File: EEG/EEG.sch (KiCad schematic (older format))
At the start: 1 part

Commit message: ...
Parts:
- gave numbers to parts that had none: 1
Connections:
- net labels added: +5V, GND
- wire segments 0 -> 3
- no-connect marks 0 -> 2
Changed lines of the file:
@@
 $EndDescr
 $Comp
-L Connector:USB_B_Micro J?
+L Connector:USB_B_Micro J1
 U 1 1 603925D3
 P 1950 2800
-F 0 "J?" H 2007 3267 50  0000 C CNN
+F 0 "J1" H 2007 3267 50  0000 C CNN
 F 1 "USB_B_Micro" H 2007 3176 50  0000 C CNN
 F 2 "" H 2100 2750 50  0001 C CNN
@@
 	1    0    0    -1
 $EndComp
+Wire Wire Line
+	1950 3200 1950 3500
+$Comp
+L power:GND #PWR?
+U 1 1 603940FA
+P 1950 3500
+F 0 "#PWR?" H 1950 3250 50  0001 C CNN
+F 1 "GND" H 1955 3327 50  0000 C CNN
+F 2 "" H 1950 3500 50  0001 C CNN
+F 3 "" H 1950 3500 50  0001 C CNN
+	1    1950 3500
+	1    0    0    -1
+$EndComp
+NoConn ~ 1850 3200
+NoConn ~ 2250 3000
+$Comp
+L power:+5V #PWR?
+U 1 1 60394FDA
+P 2500 2300
+F 0 "#PWR?" H 2500 2150 50  0001 C CNN
+F 1 "+5V" H 2515 2473 50  0000 C CNN
+F 2 "" H 2500 2300 50  0001 C CNN
+F 3 "" H 2500 2300 50  0001 C CNN
+	1    2500 2300
+	1    0    0    -1
+$EndComp
+Wire Wire Line
+	2250 2600 2500 2600
+Wire Wire Line
+	2500 2600 2500 2300
 $EndSCHEMATC

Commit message: added stuff to schematic
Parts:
- added C? (x2): 10uF, symbol Device:CP_Small
- added C? (x4): 0.1uF, symbol Device:CP_Small
- added C?: 2.2uF, symbol Device:CP_Small
- added C? (x8): 100nF, symbol Device:CP_Small
- added D? (x3): D_TVS, symbol Device:D_TVS
- added D?: LED, symbol Device:LED
- added D?: D_Schottky_Small, symbol Device:D_Schottky_Small
- added Q? (x2): 2N2219, Package_TO_SOT_THT:TO-39-3, symbol Transistor_BJT:2N2219
- added R? (x3): 2K, symbol Device:R_Small_US
- added R? (x4): 0R, symbol Device:R_Small_US
- added R? (x2): 10K, symbol Device:R_Small_US
- added SW? (x2): SW_Push, symbol Switch:SW_Push
- added U?: AMS1117-3.3, Package_TO_SOT_SMD:SOT-223-3_TabPin2, symbol Regulator_Linear:AMS1117-3.3
- added U?: FT231XS, Package_SO:SSOP-20_3.9x8.7mm_P0.635mm, symbol Interface_USB:FT231XS
- added U?: ESP32-PICO-D4, Package_DFN_QFN:QFN-48-1EP_7x7mm_P0.5mm_EP5.3x5.3mm, symbol RF_Module:ESP32-PICO-D4
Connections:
- net labels added: +3.3V, D+, D-, EN, IO0, RXD, TXD
- net labels removed: +5V
- wire segments 3 -> 145
- no-connect marks 2 -> 10
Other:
- note added: "3.3V power Supply"
- note added: "Push buttons\n"
- note added: "USB to UART\n"
- moved on the sheet: J1

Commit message: ...
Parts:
- added R?: 5k, symbol Device:R_Small_US
- added U?: MAX7219, symbol Driver_LED:MAX7219
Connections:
- net +3V3: now also R?.2, U?.19 (V+)
- net GND: now also U?.4 (GND), U?.9 (GND)
- net CS: now reaches U?.34 (IO5)
- net CS: now also U?.12 (LOAD)
- net Sclk: now reaches U?.35 (IO18)
- net Sclk: now also U?.13 (CLK)
- net Data: now reaches U?.36 (IO23)
- net Data: now also U?.1 (DIN)
- new net: R?.1, U?.18 (ISET)
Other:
- moved on the sheet: C?, R?, U?

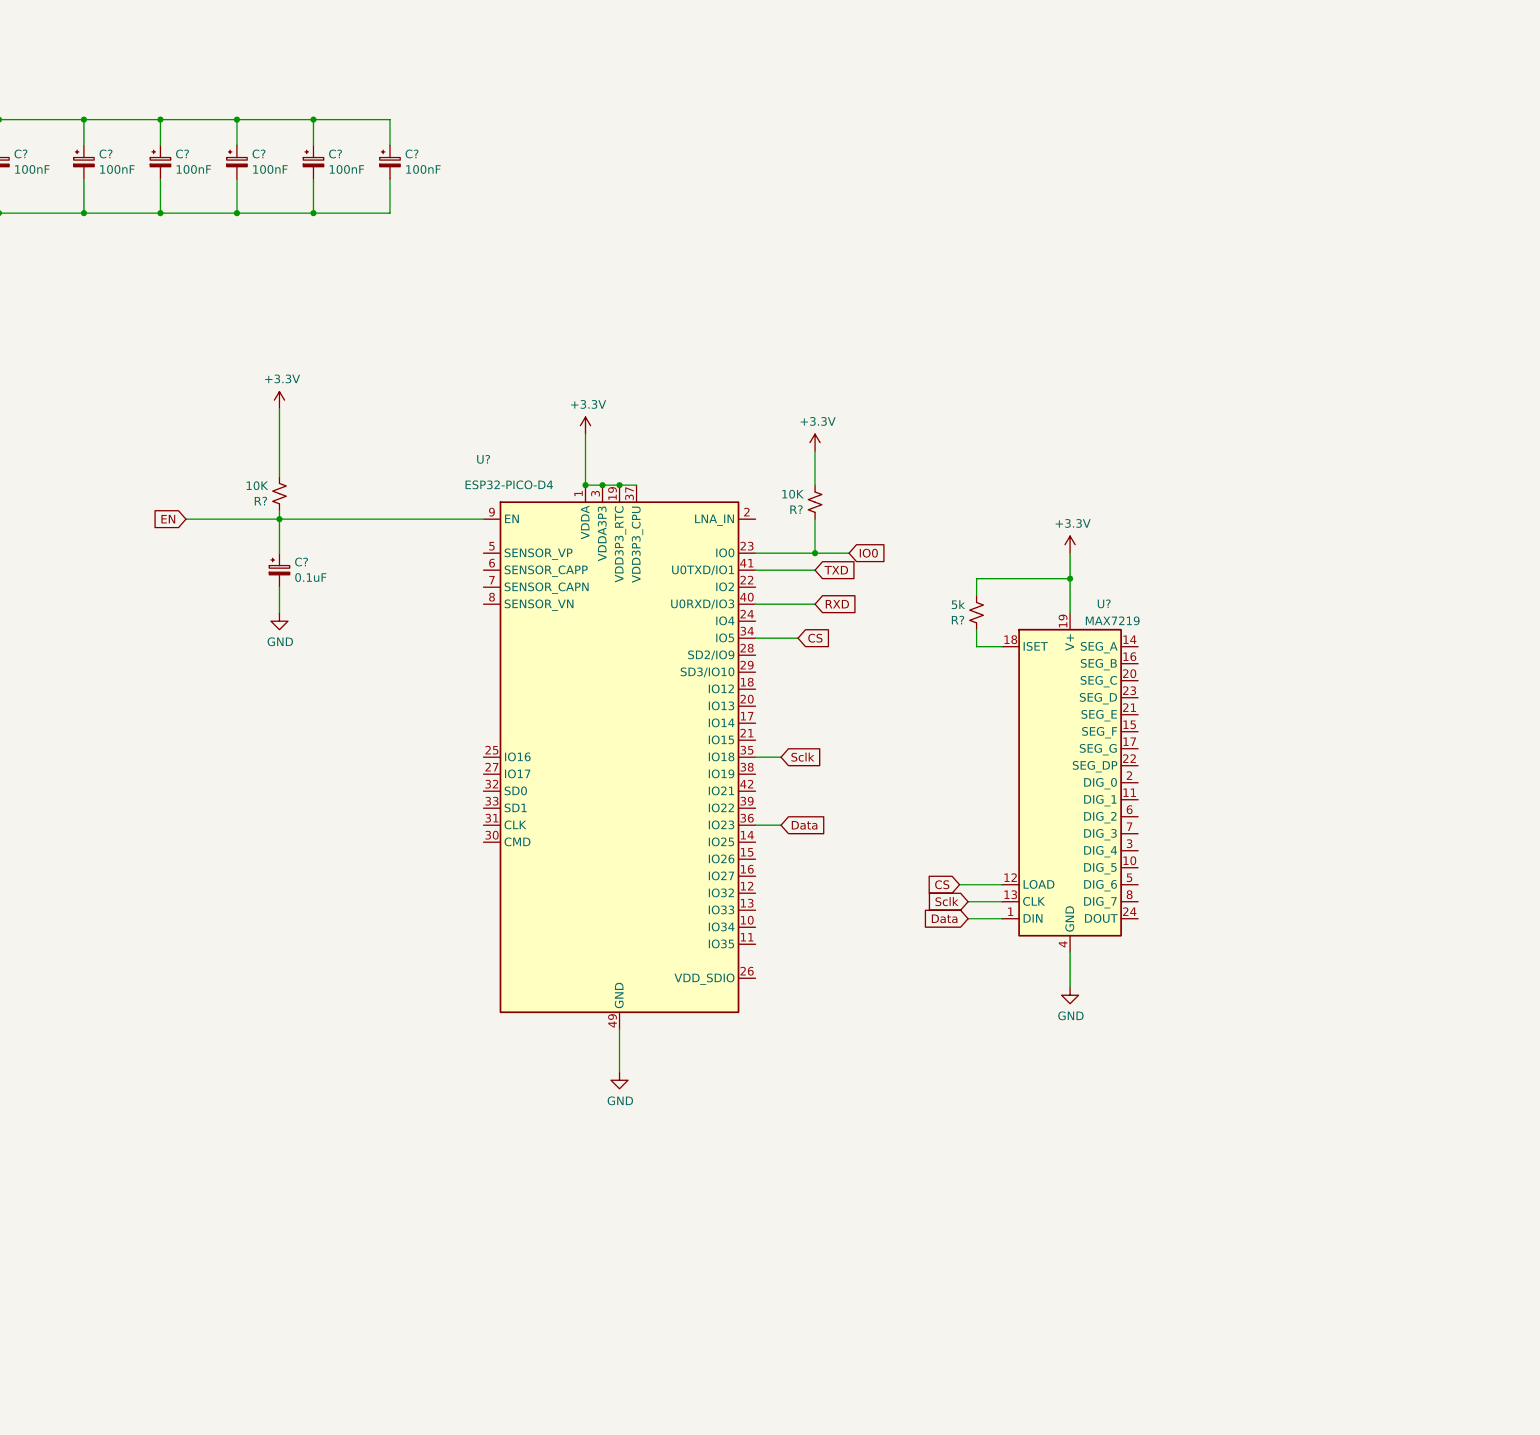
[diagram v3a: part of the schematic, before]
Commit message: ADDED LED
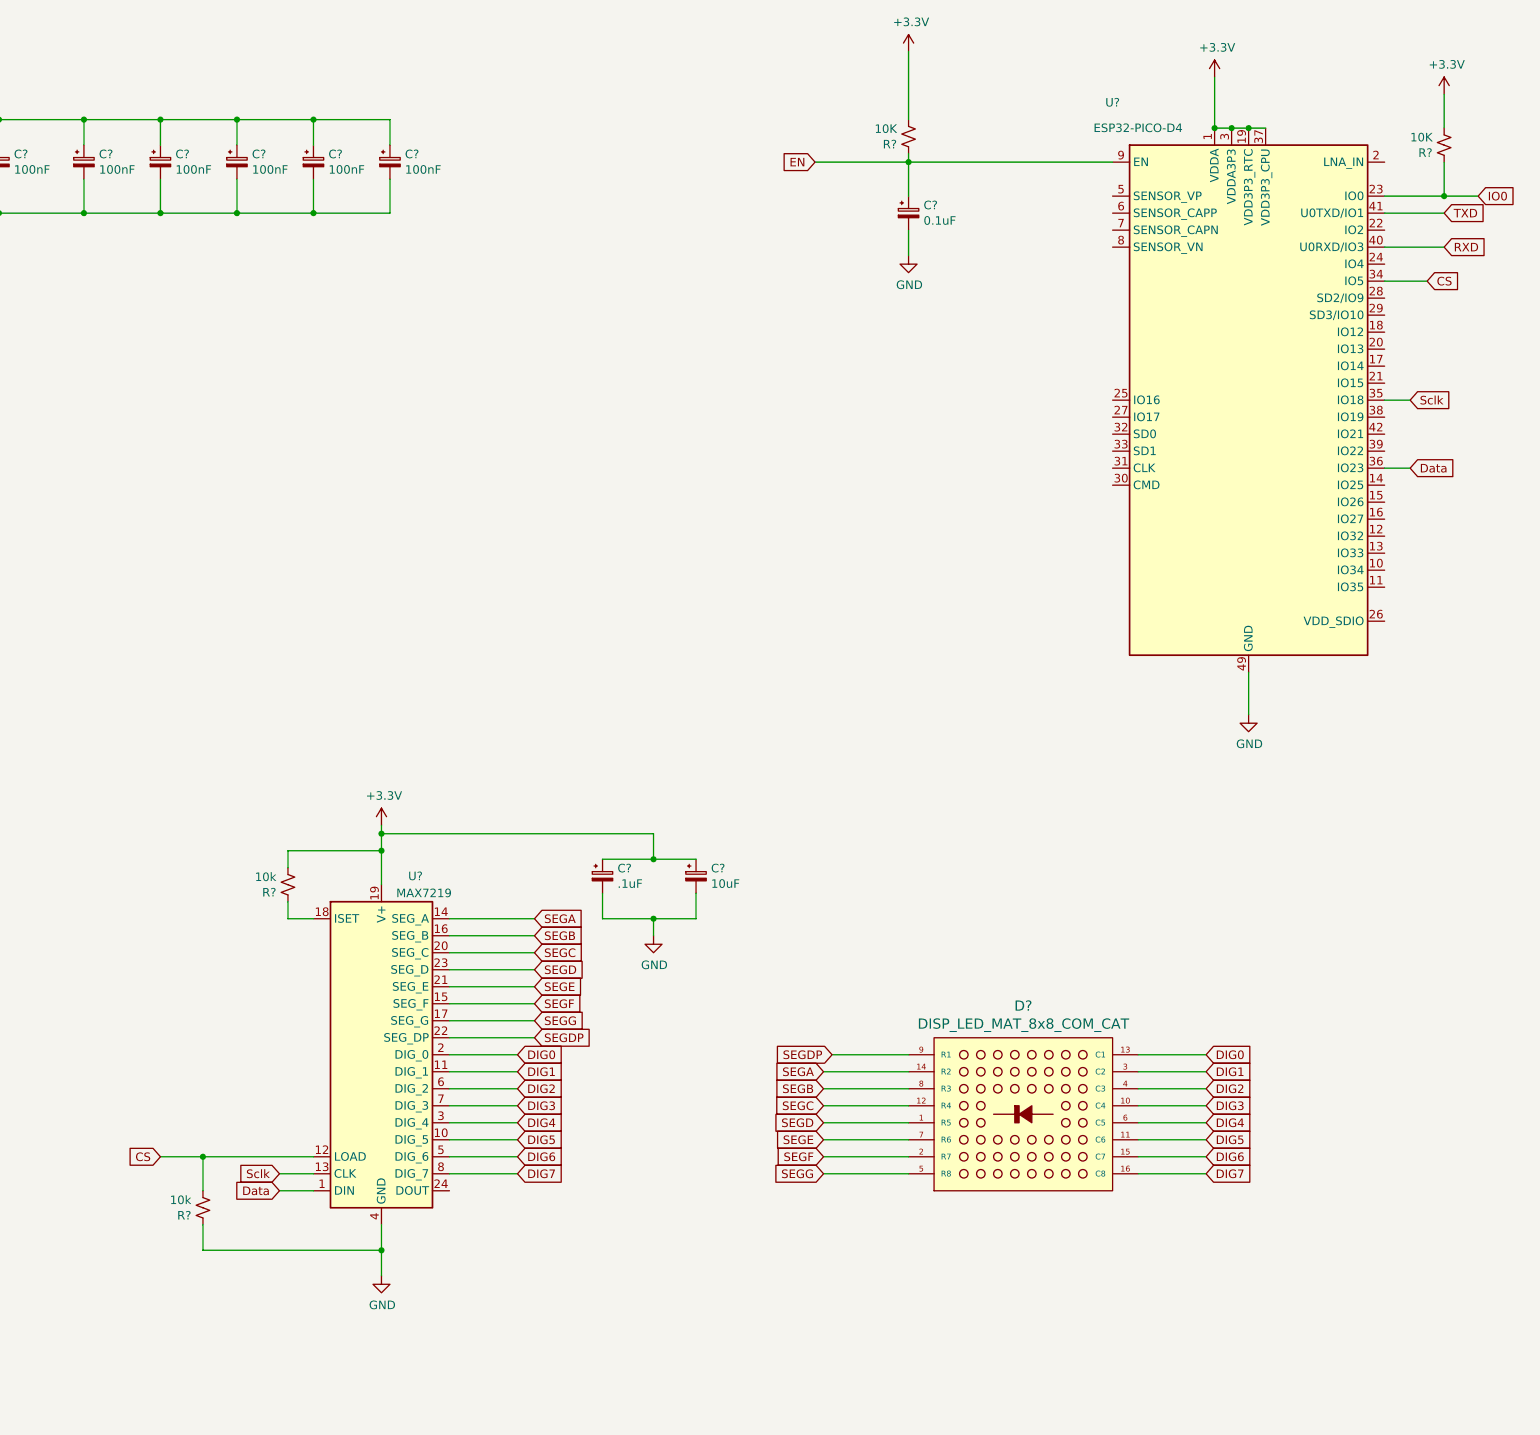
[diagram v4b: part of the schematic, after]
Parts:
- added C?: .1uF, symbol Device:CP_Small
- added C?: 10uF, symbol Device:CP_Small
- added D?: DISP_LED_MAT_8x8_COM_CAT, symbol akn_misc:DISP_LED_MAT_8x8_COM_CAT
- added R?: 10k, symbol Device:R_Small_US
- R?: value 5k -> 10k
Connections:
- net +3V3: now also C?.1, C?.1
- net CS: now also R?.2
- net GND: now also C?.2, C?.2, R?.1
- net DIG5: now reaches U?.10 (DIG_5)
- net DIG5: now also D?.11 (C6)
- net DIG1: now reaches U?.11 (DIG_1)
- net DIG1: now also D?.3 (C2)
- net SEGA: now reaches U?.14 (SEG_A)
- net SEGA: now also D?.14 (R2)
- net SEGF: now reaches U?.15 (SEG_F)
- net SEGF: now also D?.2 (R7)
- net SEGB: now reaches U?.16 (SEG_B)
- net SEGB: now also D?.8 (R3)
- net SEGG: now reaches U?.17 (SEG_G)
- net SEGG: now also D?.5 (R8)
- net DIG0: now reaches U?.2 (DIG_0)
- net DIG0: now also D?.13 (C1)
- net SEGC: now reaches U?.20 (SEG_C)
- net SEGC: now also D?.12 (R4)
- net SEGE: now reaches U?.21 (SEG_E)
- net SEGE: now also D?.7 (R6)
- net SEGDP: now reaches U?.22 (SEG_DP)
- net SEGDP: now also D?.9 (R1)
- net SEGD: now reaches U?.23 (SEG_D)
- net SEGD: now also D?.1 (R5)
- net DIG4: now reaches U?.3 (DIG_4)
- net DIG4: now also D?.6 (C5)
- net DIG6: now reaches U?.5 (DIG_6)
- net DIG6: now also D?.15 (C7)
- net DIG2: now reaches U?.6 (DIG_2)
- net DIG2: now also D?.4 (C3)
- net DIG3: now reaches U?.7 (DIG_3)
- net DIG3: now also D?.10 (C4)
- net DIG7: now reaches U?.8 (DIG_7)
- net DIG7: now also D?.16 (C8)
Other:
- moved on the sheet: C?, R?, U?

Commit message: added some footprints
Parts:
- removed D?: DISP_LED_MAT_8x8_COM_CAT, symbol akn_misc:DISP_LED_MAT_8x8_COM_CAT
- added H1, H2, H3, H4: MountingHole_Pad, symbol Mechanical:MountingHole_Pad
- added J2, J3: Conn_01x08_Female, symbol Connector:Conn_01x08_Female
- C1, C10, C11, C12, C13, C14, C15, C16, C17, C2, C3, C4, C5, C6, C7, C8, C9: renamed from C?; footprint (none) -> Capacitor_SMD:C_1206_3216Metric_Pad1.33x1.80mm_HandSolder
- D1: renamed from D?; footprint (none) -> Diode_SMD:D_1206_3216Metric_Pad1.42x1.75mm_HandSolder
- gave numbers to parts that had none: 23
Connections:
- net +3V3: now also D2.2 (A)
- net DIG0: now also J3.8 (Pin_8)
- net DIG1: now also J3.7 (Pin_7)
- net DIG2: now also J3.6 (Pin_6)
- net DIG3: now also J3.5 (Pin_5)
- net DIG4: now also J3.4 (Pin_4)
- net DIG5: now also J3.3 (Pin_3)
- net DIG6: now also J3.2 (Pin_2)
- net DIG7: now also J3.1 (Pin_1)
- net GND: now also H1.1, H2.1, H3.1, H4.1
- net SEGA: now also J2.2 (Pin_2)
- net SEGB: now also J2.3 (Pin_3)
- net SEGC: now also J2.4 (Pin_4)
- net SEGD: now also J2.5 (Pin_5)
- net SEGDP: now also J2.1 (Pin_1)
- net SEGE: now also J2.6 (Pin_6)
- net SEGF: now also J2.7 (Pin_7)
- net SEGG: now also J2.8 (Pin_8)
- net at C2.1, D1.1 (K), U1.3 (VI): no longer D2.2 (A)
- no-connect marks 10 -> 41
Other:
- note added: "8x8 LED Matrix Connectors"
- note added: "Decoupling Caps"
- note added: "ESP32-PICO-D4"
- note added: "MAX7219 LED Matrix Driver"
- note added: "Mounting Holes\n"
- moved on the sheet: C1, C10, C11, C12, C13, C14, C15, C16, C17, C4, C5, C6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
